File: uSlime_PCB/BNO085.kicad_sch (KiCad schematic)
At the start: 4 parts, among them CN1 X1502WR-05K-N0SN, U5 BNO085

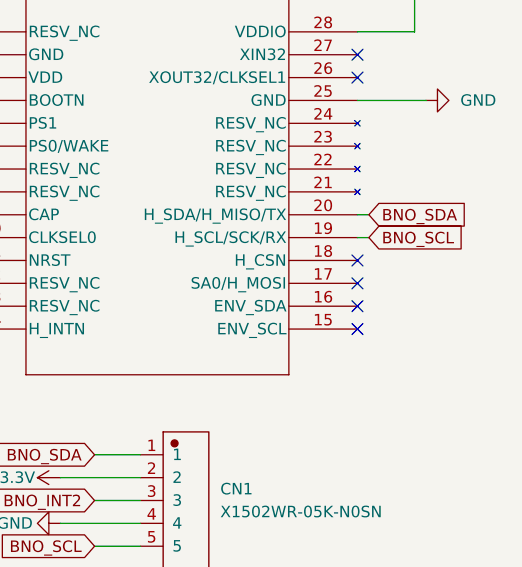
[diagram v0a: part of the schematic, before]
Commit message: Faulty BNO085 footprint
First, I do not like you UltraLibrarian anymore, for you have wasted a
lot of time and effort (and money) on footprints that are just straight
up wrong. I am this close to unleashing unbridled rage on this but will
bottle it up for now.

Second, I took the BNO085 footprint from the official SlimeVR tracker
and put it in this project. At least they have the right footprint...

Stencils for the main microcontroller does not need to change but the
extension module got a revamp in favor of being more versatile. You can
now choose which I2C address the sensor operates on; just make sure you
bridge the right contacts.
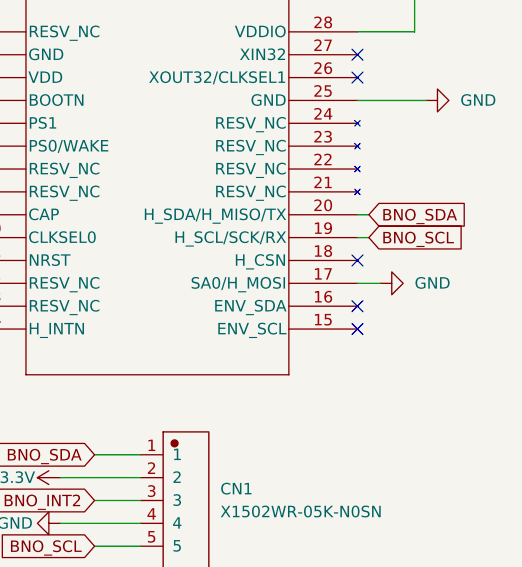
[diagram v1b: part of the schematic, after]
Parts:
- U5: footprint uSlime-libs:LGA28_5.2X3.8_CEV -> uSlime-libs:BNO080
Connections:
- net GND: now also U5.17 (SA0/H_MOSI)
- no-connect marks 10 -> 9
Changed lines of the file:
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@@
-	)
-	(no_connect
-		(at 160.02 105.41)
 	)
 	(no_connect
@@
 		(pts
 			(xy 95.25 74.93) (xy 99.06 74.93)
+		)
+		(stroke
+			(width 0)
+			(type default)
+		)
+	)
+	(wire
+		(pts
+			(xy 162.56 105.41) (xy 160.02 105.41)
 		)
 		(stroke
@@
 			)
 		)
-		(property "Footprint" "uSlime-libs:LGA28_5.2X3.8_CEV"
+		(property "Footprint" "uSlime-libs:BNO080"
 			(at 115.57 77.47 0)
 			(effects
@@
 					(unit 1)
 				)
+			)
+		)
+	)
+	(symbol
+		(lib_id "power:GND")
+		(at 162.56 105.41 90)
+		(unit 1)
+		(exclude_from_sim no)
+		(in_bom yes)
+		(on_board yes)
+		(dnp no)
+		(fields_autoplaced yes)
+		(property "Reference" "#PWR013"
+			(at 168.91 105.41 0)
+			(effects
+				(font
+					(size 1.27 1.27)
+				)
+				(hide yes)
+			)
+		)
+		(property "Value" "GND"
+			(at 166.37 105.4099 90)
+			(effects
+				(font
+					(size 1.27 1.27)
+				)
+				(justify right)
+			)
+		)
+		(property "Footprint" ""
+			(at 162.56 105.41 0)
+			(effects
+				(font
+					(size 1.27 1.27)
+				)
+				(hide yes)
+			)
+		)
+		(property "Datasheet" ""
+			(at 162.56 105.41 0)
+			(effects
+				(font
+					(size 1.27 1.27)
+				)
+				(hide yes)
+			)
+		)
+		(property "Description" "Power symbol creates a global label with name \"GND\" , ground"
+			(at 162.56 105.41 0)
+			(effects
+				(font
+					(size 1.27 1.27)
+				)
+				(hide yes)
+			)
+		)
+		(pin "1"
+		)
+		(instances
+			(project "uSlime"
+				(path "/f32c1c49-f803-4e7c-a530-6db148a7ba36/1072de81-ddaf-4115-9b1e-8b480e2a0117"
+					(reference "#PWR013")
+					(unit 1)
+				)

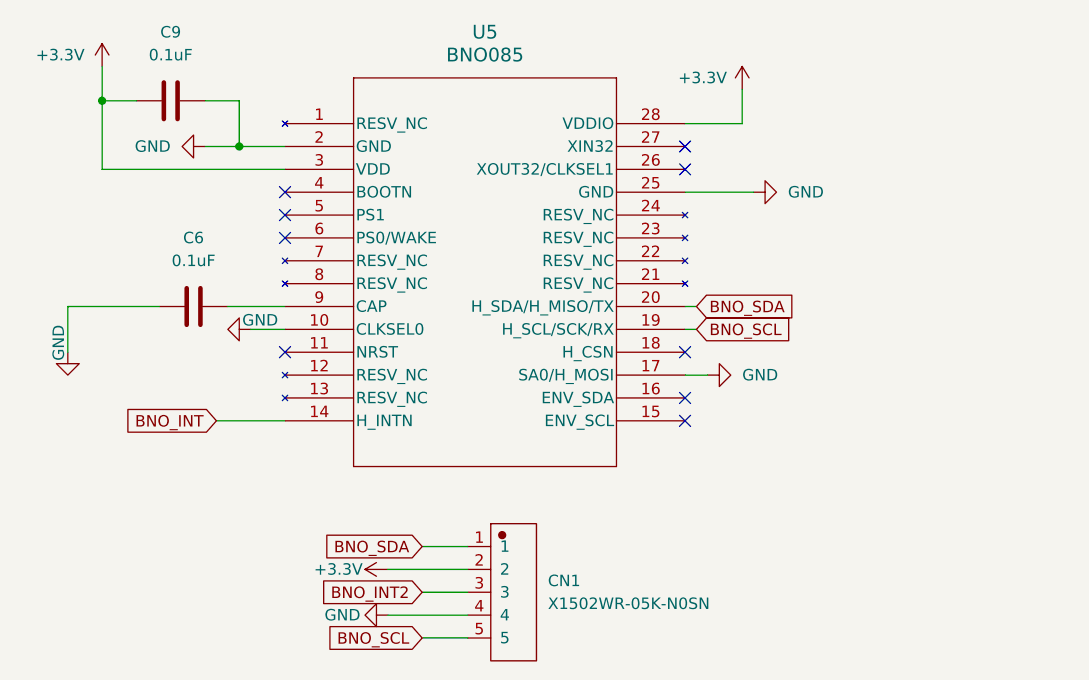
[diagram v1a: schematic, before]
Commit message: update selection i2c
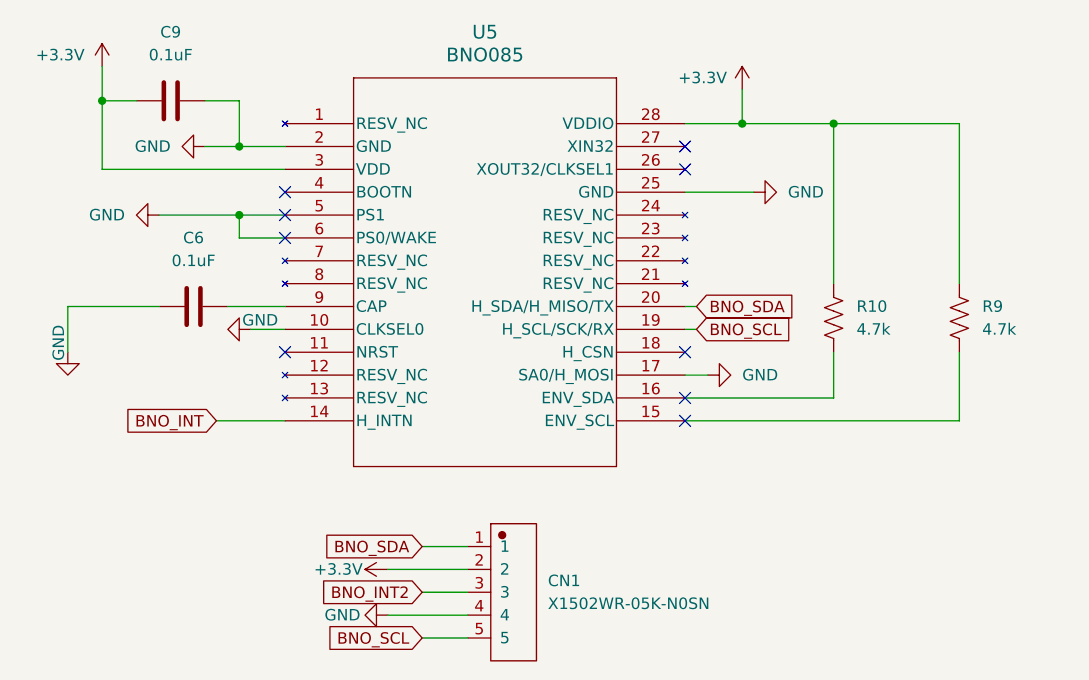
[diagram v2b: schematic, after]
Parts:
- added R10, R9: 4.7k, Resistor_SMD:R_0402_1005Metric, symbol uSlime:R_US
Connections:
- net +3.3V: now also R10.1, R9.1
- net GND: now also U5.5 (PS1), U5.6 (PS0/WAKE)
- net at U5.15 (ENV_SCL): now also R9.2
- net at U5.16 (ENV_SDA): now also R10.2

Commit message: Update main board BNO
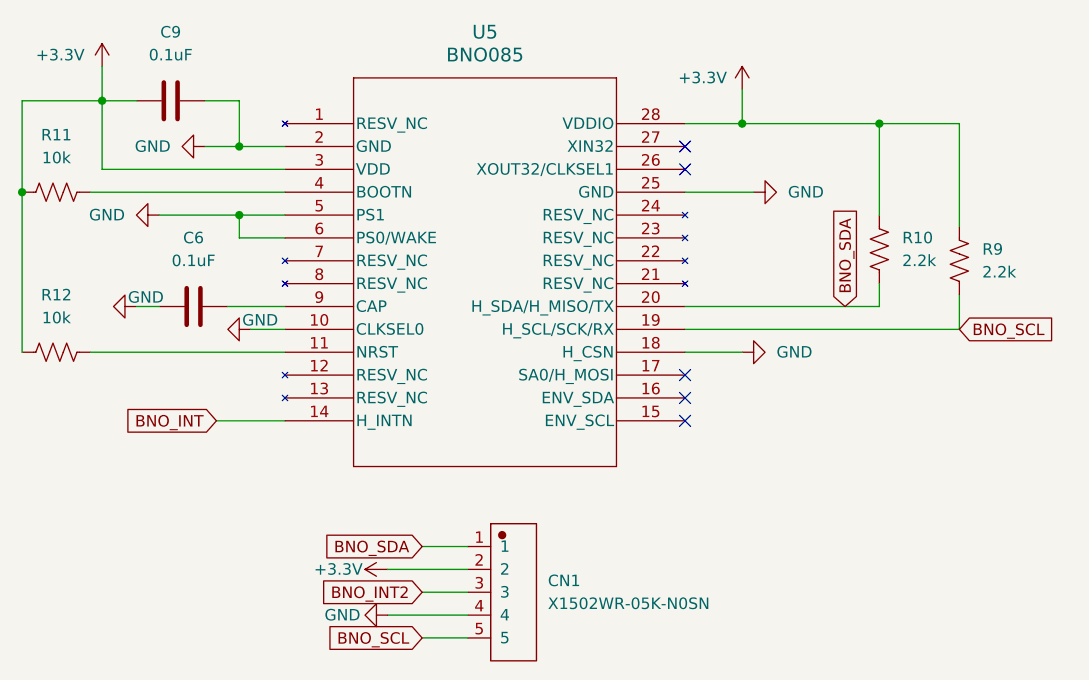
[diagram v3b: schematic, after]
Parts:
- added R11, R12: 10k, Resistor_SMD:R_0402_1005Metric, symbol uSlime:R_US
- R10, R9: value 4.7k -> 2.2k
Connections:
- net +3.3V: now also R11.1, R12.2
- net BNO_SCL: now also R9.2
- net BNO_SDA: now also R10.2
- net GND: now also U5.18 (H_CSN); no longer U5.17 (SA0/H_MOSI)
- net at U5.15 (ENV_SCL): no longer R9.2
- net at U5.16 (ENV_SDA): no longer R10.2
- net at U5.11 (NRST): now also R12.1
- net at U5.4 (BOOTN): now also R11.2
- no-connect marks 9 -> 5
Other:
- moved on the sheet: R10, R9

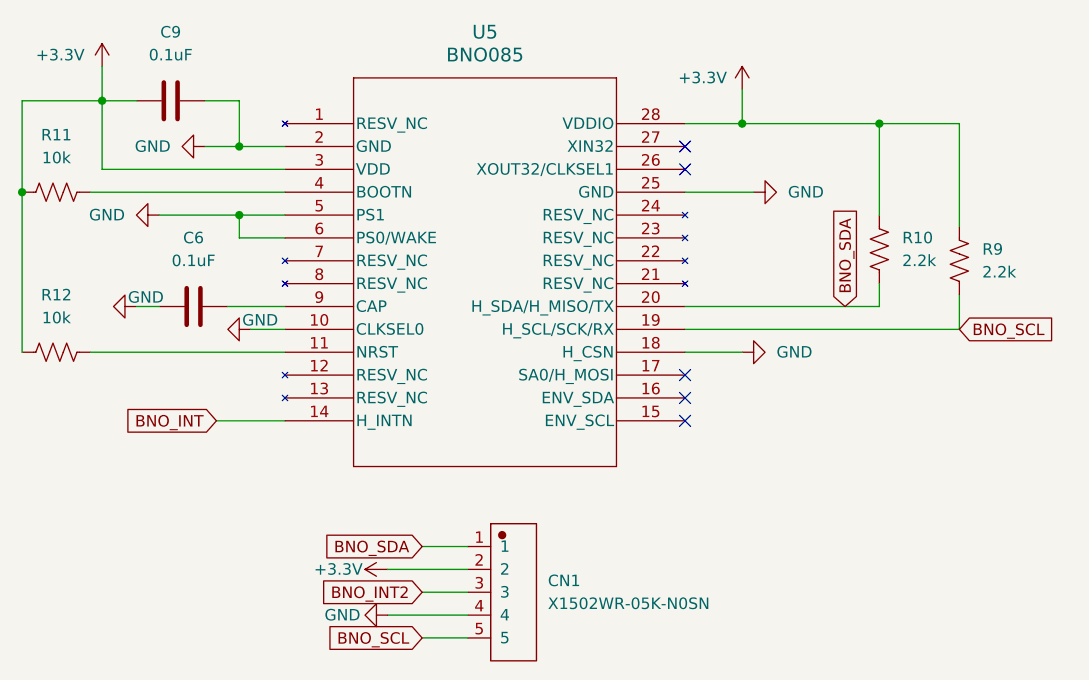
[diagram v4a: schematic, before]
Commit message: v0.0.3a Fix wrong I2C address for 0x4A
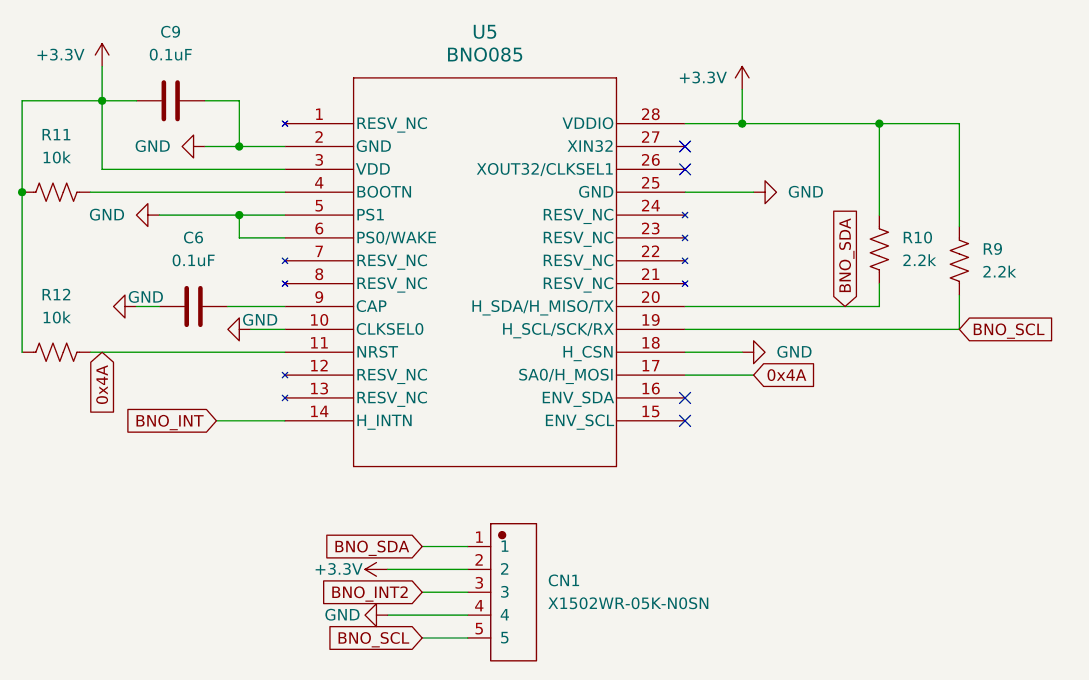
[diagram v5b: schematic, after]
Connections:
- net 0x4A: now reaches R12.1, U5.11 (NRST)
- net 0x4A: now also U5.17 (SA0/H_MOSI)
- no-connect marks 5 -> 4
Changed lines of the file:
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@@
-	)
-	(no_connect
-		(at 160.02 105.41)
 	)
 	(no_connect
@@
 	(wire
 		(pts
+			(xy 160.02 105.41) (xy 167.64 105.41)
+		)
+		(stroke
+			(width 0)
+			(type default)
+		)
+	)
+	(wire
+		(pts
 			(xy 190.5 77.47) (xy 181.61 77.47)
 		)
@@
 		)
 	)
+	(global_label "0x4A"
+		(shape input)
+		(at 95.25 102.87 270)
+		(fields_autoplaced yes)
+		(effects
+			(font
+				(size 1.27 1.27)
+			)
+			(justify right)
+		)
+		(property "Intersheetrefs" "${INTERSHEET_REFS}"
+			(at 95.25 110.3909 90)
+			(effects
+				(font
+					(size 1.27 1.27)
+				)
+				(justify right)
+				(hide yes)
+			)
+		)
+	)
 	(global_label "BNO_SCL"
 		(shape input)
@@
 				(hide yes)
 			)
+		)
+	)
+	(global_label "0x4A"
+		(shape input)
+		(at 167.64 105.41 0)
+		(fields_autoplaced yes)
+		(effects
+			(font
+				(size 1.27 1.27)
+			)
+			(justify left)
+		)
+		(property "Intersheetrefs" "${INTERSHEET_REFS}"
+			(at 175.1609 105.41 0)
+			(effects
+				(font
+					(size 1.27 1.27)
+				)
+				(justify left)
+				(hide yes)
+			)

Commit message: Connect DI without resistor
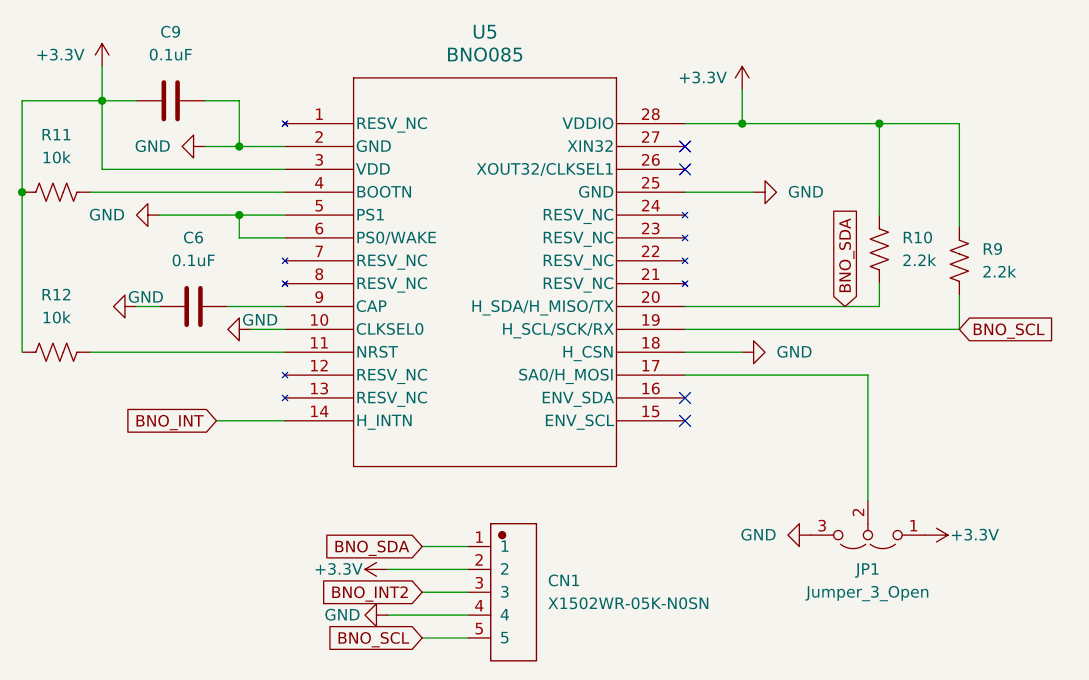
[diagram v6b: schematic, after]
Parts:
- added JP1: Jumper_3_Open, Jumper:SolderJumper-3_P1.3mm_Open_RoundedPad1.0x1.5mm, symbol uSlime:Jumper_3_Open
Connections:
- net +3.3V: now also JP1.1 (A)
- net GND: now also JP1.3 (B)
- net 0x4A: no longer names the net of R12.1, U5.11 (NRST)
- net 0x4A: no longer U5.17 (SA0/H_MOSI)
- new net: JP1.2 (C), U5.17 (SA0/H_MOSI)
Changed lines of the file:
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@@
+	(wire
+		(pts
+			(xy 180.34 105.41) (xy 180.34 119.38)
+		)
+		(stroke
+			(width 0)
+			(type default)
+		)
+	)
 	(wire
 		(pts
@@
 	(wire
 		(pts
-			(xy 160.02 105.41) (xy 167.64 105.41)
+			(xy 160.02 105.41) (xy 180.34 105.41)
 		)
 		(stroke
@@
 		)
 	)
-	(global_label "0x4A"
+	(global_label "BNO_SCL"
 		(shape input)
-		(at 95.25 102.87 270)
+		(at 130.81 134.62 180)
 		(fields_autoplaced yes)
 		(effects
@@
 		)
 		(property "Intersheetrefs" "${INTERSHEET_REFS}"
-			(at 95.25 110.3909 90)
+			(at 119.4186 134.62 0)
 			(effects
 				(font
@@
 		)
 	)
-	(global_label "BNO_SCL"
+	(global_label "BNO_INT"
 		(shape input)
-		(at 130.81 134.62 180)
+		(at 107.95 110.49 180)
 		(fields_autoplaced yes)
 		(effects
@@
 		)
 		(property "Intersheetrefs" "${INTERSHEET_REFS}"
-			(at 119.4186 134.62 0)
+			(at 97.1633 110.49 0)
 			(effects
 				(font
@@
 		)
 	)
-	(global_label "0x4A"
+	(global_label "BNO_SDA"
 		(shape input)
-		(at 167.64 105.41 0)
+		(at 177.8 97.79 90)
 		(fields_autoplaced yes)
 		(effects
@@
 		)
 		(property "Intersheetrefs" "${INTERSHEET_REFS}"
-			(at 175.1609 105.41 0)
-			(effects
-				(font
-					(size 1.27 1.27)
-				)
-				(justify left)
-				(hide yes)
-			)
-		)
-	)
-	(global_label "BNO_INT"
-		(shape input)
-		(at 107.95 110.49 180)
-		(fields_autoplaced yes)
-		(effects
-			(font
-				(size 1.27 1.27)
-			)
-			(justify right)
-		)
-		(property "Intersheetrefs" "${INTERSHEET_REFS}"
-			(at 97.1633 110.49 0)
-			(effects
-				(font
-					(size 1.27 1.27)
-				)
-				(justify right)
-				(hide yes)
-			)
-		)
-	)
-	(global_label "BNO_SDA"
-		(shape input)
-		(at 177.8 97.79 90)
-		(fields_autoplaced yes)
-		(effects
-			(font
-				(size 1.27 1.27)
-			)
-			(justify left)
-		)
-		(property "Intersheetrefs" "${INTERSHEET_REFS}"
 			(at 177.8 86.3381 90)
 			(effects
@@
 	)
 	(symbol
+		(lib_id "uSlime:Jumper_3_Open")
+		(at 180.34 123.19 180)
+		(unit 1)
+		(exclude_from_sim yes)
+		(in_bom no)
+		(on_board yes)
+		(dnp no)
+		(fields_autoplaced yes)
+		(property "Reference" "JP1"
+			(at 180.34 127 0)
+			(effects
+				(font
+					(size 1.27 1.27)
+				)
+			)
+		)
+		(property "Value" "Jumper_3_Open"
+			(at 180.34 129.54 0)
+			(effects
+				(font
+					(size 1.27 1.27)
+				)
+			)
+		)
+		(property "Footprint" "Jumper:SolderJumper-3_P1.3mm_Open_RoundedPad1.0x1.5mm"
+			(at 180.34 123.19 0)
+			(effects
+				(font
+					(size 1.27 1.27)
+				)
+				(hide yes)
+			)
+		)
+		(property "Datasheet" "~"
+			(at 180.34 123.19 0)
+			(effects
+				(font
+					(size 1.27 1.27)
+				)
+				(hide yes)
+			)
+		)
+		(property "Description" "Jumper, 3-pole, both open"
+			(at 180.34 123.19 0)
+			(effects
+				(font
+					(size 1.27 1.27)
+				)
+				(hide yes)
+			)
+		)
+		(pin "1"
+		)
+		(pin "3"
+		)
+		(pin "2"
+		)
+		(instances
+			(project "uSlime"
+				(path "/f32c1c49-f803-4e7c-a530-6db148a7ba36/1072de81-ddaf-4115-9b1e-8b480e2a0117"
+					(reference "JP1")
+					(unit 1)
+				)
+			)
+		)
+	)
+	(symbol
 		(lib_id "power:GND")
 		(at 166.37 102.87 90)
@@
 	(symbol
 		(lib_id "power:GND")
-		(at 167.64 85.09 90)
+		(at 173.99 123.19 270)
 		(unit 1)
 		(exclude_from_sim no)
@@
 		(dnp no)
 		(fields_autoplaced yes)
+		(property "Reference" "#PWR023"
+			(at 167.64 123.19 0)
+			(effects
+				(font
+					(size 1.27 1.27)
+				)
+				(hide yes)
+			)
+		)
+		(property "Value" "GND"
+			(at 170.18 123.1899 90)
+			(effects
+				(font
+					(size 1.27 1.27)
+				)
+				(justify right)
+			)
+		)
+		(property "Footprint" ""
+			(at 173.99 123.19 0)
+			(effects
+				(font
+					(size 1.27 1.27)
+				)
+				(hide yes)
+			)
+		)
+		(property "Datasheet" ""
+			(at 173.99 123.19 0)
+			(effects
+				(font
+					(size 1.27 1.27)
+				)
+				(hide yes)
+			)
+		)
+		(property "Description" "Power symbol creates a global label with name \"GND\" , ground"
+			(at 173.99 123.19 0)
+			(effects
+				(font
+					(size 1.27 1.27)
+				)
+				(hide yes)
+			)
+		)
+		(pin "1"
+		)
+		(instances
+			(project "uSlime"
+				(path "/f32c1c49-f803-4e7c-a530-6db148a7ba36/1072de81-ddaf-4115-9b1e-8b480e2a0117"
+					(reference "#PWR023")
+					(unit 1)
+				)
+			)
+		)
+	)
+	(symbol
+		(lib_id "power:GND")
+		(at 167.64 85.09 90)
+		(unit 1)
+		(exclude_from_sim no)
+		(in_bom yes)
+		(on_board yes)
+		(dnp no)
+		(fields_autoplaced yes)
 		(property "Reference" "#PWR09"
 			(at 173.99 85.09 0)
@@
 					(unit 1)
 				)
+			)
+		)
+	)
+	(symbol
+		(lib_id "power:+3.3V")
+		(at 186.69 123.19 270)
+		(unit 1)
+		(exclude_from_sim no)
+		(in_bom yes)
+		(on_board yes)
+		(dnp no)
+		(property "Reference" "#PWR024"
+			(at 182.88 123.19 0)
+			(effects
+				(font
+					(size 1.27 1.27)
+				)
+				(hide yes)
+			)
+		)
+		(property "Value" "+3.3V"
+			(at 189.484 123.19 90)
+			(effects
+				(font
+					(size 1.27 1.27)
+				)
+				(justify left)
+			)
+		)
+		(property "Footprint" ""
+			(at 186.69 123.19 0)
+			(effects
+				(font
+					(size 1.27 1.27)
+				)
+				(hide yes)
+			)
+		)
+		(property "Datasheet" ""
+			(at 186.69 123.19 0)
+			(effects
+				(font
+					(size 1.27 1.27)
+				)
+				(hide yes)
+			)
+		)
+		(property "Description" "Power symbol creates a global label with name \"+3.3V\""
+			(at 186.69 123.19 0)
+			(effects
+				(font
+					(size 1.27 1.27)
+				)
+				(hide yes)
+			)
+		)
+		(pin "1"
+		)
+		(instances
+			(project "uSlime"
+				(path "/f32c1c49-f803-4e7c-a530-6db148a7ba36/1072de81-ddaf-4115-9b1e-8b480e2a0117"
+					(reference "#PWR024")
+					(unit 1)
+				)
